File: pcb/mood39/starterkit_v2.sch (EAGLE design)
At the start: 18 parts, among them IC1 TINY85, IC2 LM2940, X1 PWRUSB, X3 PWRUNREG

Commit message: teile ersetzt durch tatsächlich verfügbare
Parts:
- removed X3: PWRUNREG, con-wago-500:W237-102
- added U$1: RIACON_101_2, n39:RIACON_101_2
- R5: value EVUF2A -> ALPS_RK09K113; device pot:EVUF2A -> n39:ALPS_RK09K113
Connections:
- new net !RESET: IC1.RESET, R1.2
- net GND: now also U$1.1; no longer X3-1.KL
- net V+: now also U$1.2; no longer X3-2.KL
- net _RESET: no longer IC1.RESET, R1.2
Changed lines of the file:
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@@
 <part name="X1" library="con-berg" deviceset="PN61729" device="" value="PWRUSB"/>
 <part name="IC2" library="v-reg" deviceset="78XXS" device="" value="LM2940"/>
-<part name="X3" library="con-wago-500" deviceset="W237-102" device="" value="PWRUNREG"/>
 <part name="C2" library="rcl" deviceset="CPOL-EU" device="E2.5-5" value="47u"/>
 <part name="C3" library="rcl" deviceset="C-EU" device="C0805" value="470n"/>
-<part name="R5" library="pot" deviceset="EVU" device="A" technology="F2"/>
+<part name="R5" library="n39" deviceset="ALPS_RK09K113" device=""/>
 <part name="JP1" library="pinhead" deviceset="PINHD-1X1" device="" value="I2CDAT"/>
 <part name="GND2" library="supply1" deviceset="GND" device=""/>
@@
 <part name="R6" library="rcl" deviceset="R-EU_" device="R0805" value="1.5k"/>
 <part name="S1" library="switch-omron" deviceset="10-XX" device=""/>
+<part name="U$1" library="n39" deviceset="RIACON_101_2" device=""/>
 </parts>
 <sheets>
@@
 <instance part="X1" gate="G$1" x="93.98" y="27.94" rot="R180"/>
 <instance part="IC2" gate="1" x="-5.08" y="78.74"/>
-<instance part="X3" gate="-1" x="-25.4" y="38.1"/>
-<instance part="X3" gate="-2" x="-25.4" y="78.74"/>
 <instance part="C2" gate="G$1" x="7.62" y="66.04"/>
 <instance part="C3" gate="G$1" x="-17.78" y="66.04"/>
@@
 <instance part="R6" gate="G$1" x="30.48" y="50.8"/>
 <instance part="S1" gate="1" x="73.66" y="43.18" rot="R270"/>
+<instance part="U$1" gate="G$1" x="-30.48" y="76.2" rot="R180"/>
 </instances>
 <busses>
@@
 <junction x="137.16" y="45.72"/>
 <junction x="137.16" y="55.88"/>
-<wire x1="-20.32" y1="38.1" x2="-17.78" y2="38.1" width="0.1524" layer="91"/>
 <pinref part="IC2" gate="1" pin="GND"/>
 <wire x1="-17.78" y1="38.1" x2="-5.08" y2="38.1" width="0.1524" layer="91"/>
@@
 <wire x1="38.1" y1="40.64" x2="38.1" y2="38.1" width="0.1524" layer="91"/>
 <junction x="38.1" y="38.1"/>
-<pinref part="X3" gate="-1" pin="KL"/>
 <pinref part="S1" gate="1" pin="P"/>
 <wire x1="68.58" y1="43.18" x2="63.5" y2="43.18" width="0.1524" layer="91"/>
@@
 <junction x="63.5" y="40.64"/>
 <junction x="63.5" y="38.1"/>
+<pinref part="U$1" gate="G$1" pin="1"/>
+<wire x1="-25.4" y1="76.2" x2="-22.86" y2="76.2" width="0.1524" layer="91"/>
+<wire x1="-22.86" y1="76.2" x2="-22.86" y2="38.1" width="0.1524" layer="91"/>
+<wire x1="-22.86" y1="38.1" x2="-17.78" y2="38.1" width="0.1524" layer="91"/>
 </segment>
 <segment>
@@
 <label x="66.04" y="30.48" size="1.778" layer="95"/>
 </segment>
-<segment>
-<pinref part="R1" gate="G$1" pin="2"/>
-<wire x1="27.94" y1="66.04" x2="27.94" y2="63.5" width="0.1524" layer="91"/>
-<pinref part="IC1" gate="G$1" pin="RESET"/>
-<wire x1="27.94" y1="63.5" x2="38.1" y2="63.5" width="0.1524" layer="91"/>
-<label x="30.48" y="63.5" size="1.778" layer="95"/>
-</segment>
 </net>
 <net name="N$5" class="2">
@@
 <wire x1="-17.78" y1="68.58" x2="-17.78" y2="78.74" width="0.1524" layer="91"/>
 <label x="-15.24" y="78.74" size="1.778" layer="95"/>
-<pinref part="X3" gate="-2" pin="KL"/>
-<wire x1="-20.32" y1="78.74" x2="-17.78" y2="78.74" width="0.1524" layer="91"/>
+<wire x1="-25.4" y1="78.74" x2="-17.78" y2="78.74" width="0.1524" layer="91"/>
 <junction x="-17.78" y="78.74"/>
+<pinref part="U$1" gate="G$1" pin="2"/>
 </segment>
 </net>
@@
 </segment>
 </net>
+<net name="!RESET" class="2">
+<segment>
+<pinref part="R1" gate="G$1" pin="2"/>
+<wire x1="27.94" y1="66.04" x2="27.94" y2="63.5" width="0.1524" layer="91"/>
+<pinref part="IC1" gate="G$1" pin="RESET"/>
+<wire x1="27.94" y1="63.5" x2="38.1" y2="63.5" width="0.1524" layer="91"/>
+<label x="30.48" y="63.5" size="1.778" layer="95"/>
+</segment>
+</net>

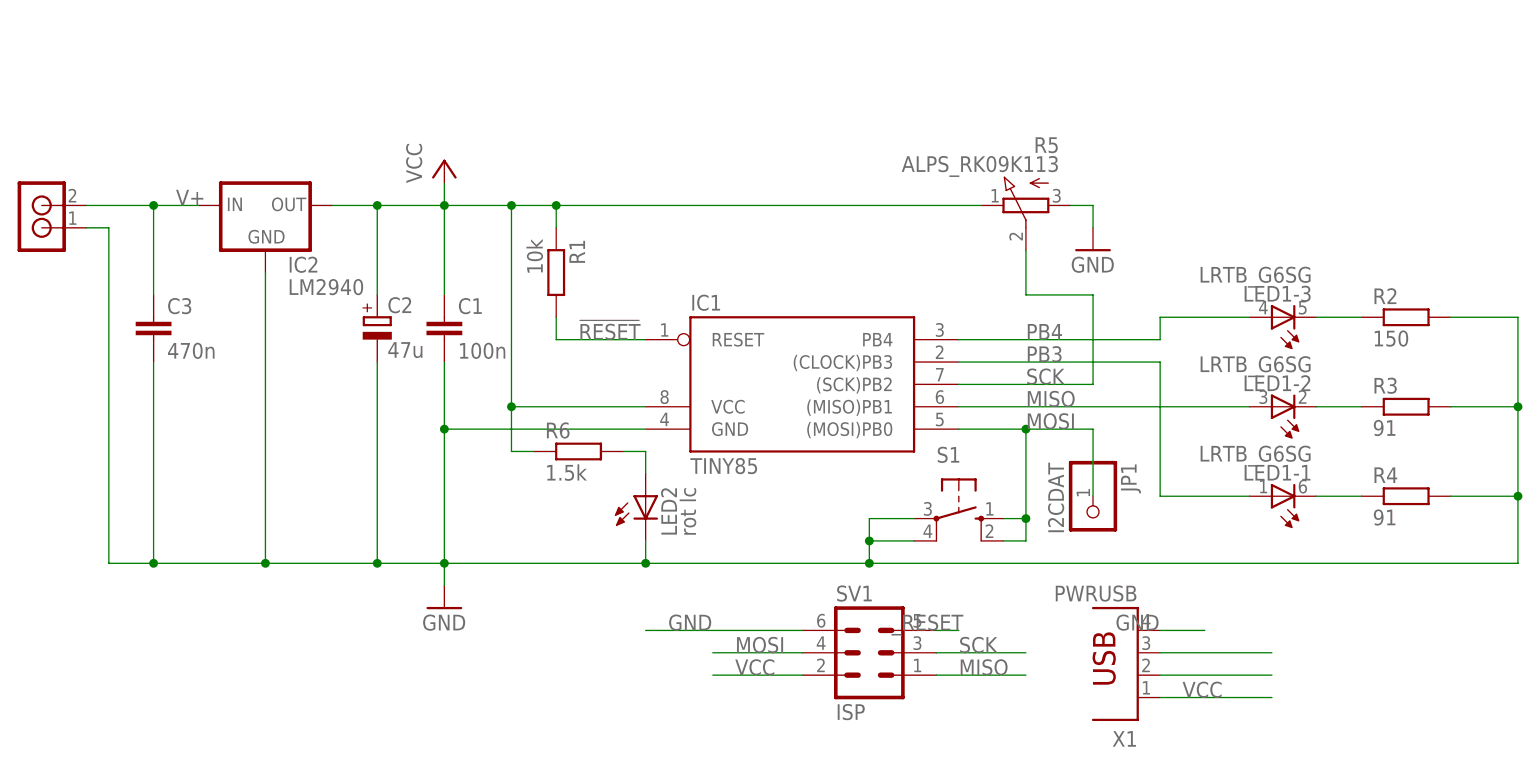
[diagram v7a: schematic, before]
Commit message: Taster ersetzt
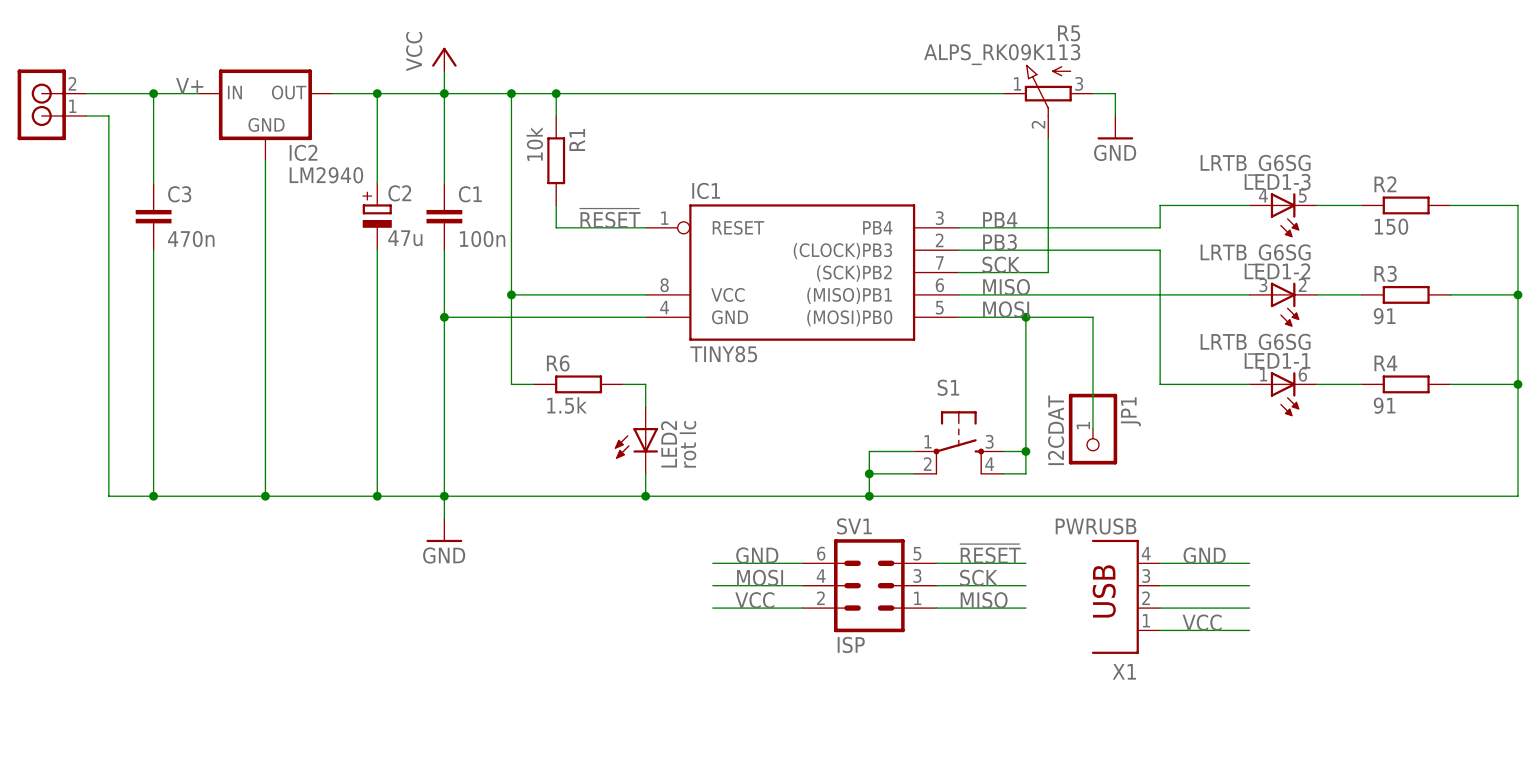
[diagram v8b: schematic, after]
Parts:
- S1: value (none) -> JTP-1130C; device switch-omron:10-XX -> n39:JTP-1130C
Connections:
- removed net _RESET: SV1.5
- net !RESET: now also SV1.5
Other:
- moved on the sheet: C1, C2, C3, IC1, IC2, JP1, LED1-1, LED1-2, LED1-3, LED2, R1, R2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
